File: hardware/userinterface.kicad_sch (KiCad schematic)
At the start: 16 parts, among them J3 NHD-2.4-240320AF-CSXP, SW3 L-KLS4-EC1121S-E5A-F12.5, U7 TPS61023DRLR, U8 CAT4104V-GT3

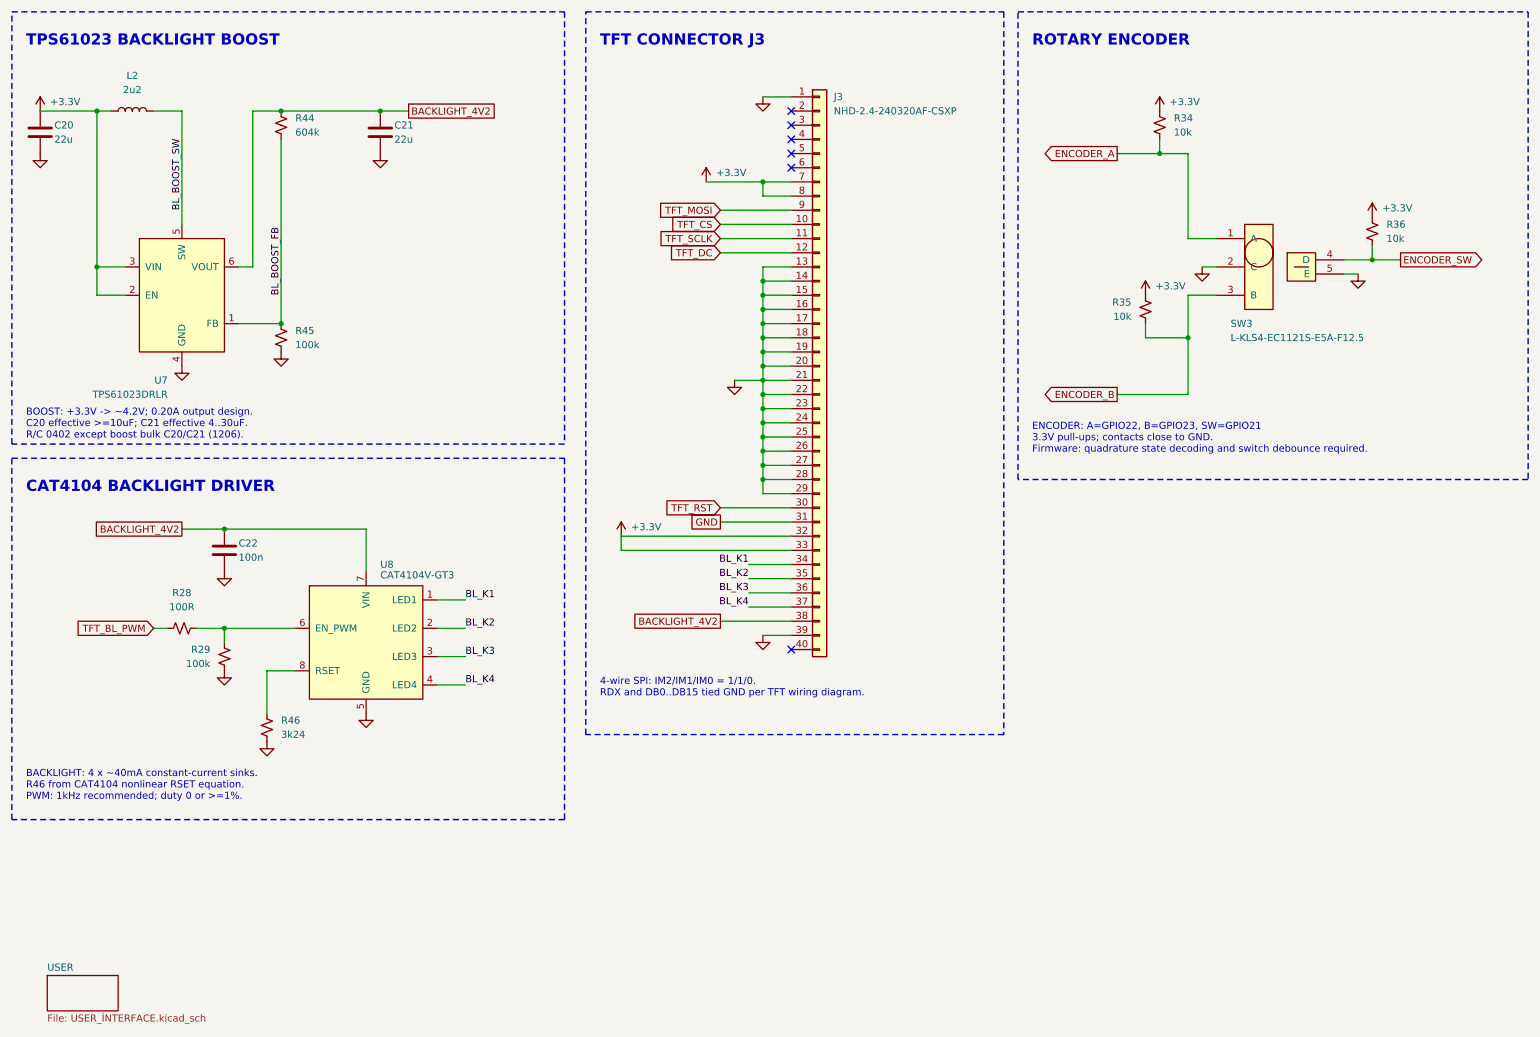
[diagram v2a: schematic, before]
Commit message: hardware: ekranı TFT032B018'e geçir, todo'yu güncelle, Imax 3 A kararını kaydet
TFT032B018 (userinterface):
- J3 Conn_01x40 (Molex 54132-4062) -> Conn_01x30, KLS L-KLS1-242I-2.0-30-R;
  yeni footprint Connector_FPC_Custom:KLS_L-KLS1-242I-2.0-30_1x30-2MP_P0.50mm_Horizontal
  (fp-lib-table'a eklendi). SPI: 16=DC, 17=SCLK, 18=CS, 19=MOSI, 20=RST;
  21 IM=3.3V; DB0..7, RDX GND; TE ve dokunmatik pinleri boş. C34 1u0 dekuplaj.
- Backlight: TPS61023 boost (U7, L2, C20, C21, R44, R45) ve CAT4104 (U8,
  C22, R46) kalktı; +3.3V -> R60 5R6 -> BL_A, BL_K -> Q7 IRLML6344
  (R28/R29 ile TFT_BL_PWM).
- Beklenen netlist farkı: BACKLIGHT_4V2, BL_BOOST_*, BL_K1..4, Net-(U8-*)
  kalktı; BL_A, BL_K, Net-(Q7-G) eklendi; TFT_* netleri J3'ün yeni pin
  numaralarına geçti. ERC değişmedi (0 hata, 2 eski uyarı).
- Özdisan alanları (J3, Q7, R60, C34) ve BOM tablosu güncellendi; ekran modülü
  şema dışı satır olarak BOM'da (stok 5).
- mcu/userinterface: kullanılmayan lib_symbols tanımları silindi
  (Device:Battery_Cell, AO3400A); netlist farkı YOK.

Kayıtlar:
- todo.txt: tamamlanan şema maddeleri
  design_decisions/output/SEMA_TAMAMLANAN_TODO_REV_C_20260922.md'ye taşındı;
  AP74502Q sembolü Diodes datasheet'iyle doğrulandı (datasheet eklendi),
  U12 paket (SOT28) kontrolü ve SMBJ30A PCB maddesi güncellendi.
- Maksimum çıkış akımı 3 A: design_decisions/output/CIKIS_AKIMI_3A_KARARI_20260922.md.
  "Imax kesinleştir" ve "3.3 V adaptör başlığı" maddeleri kapandı; prototip ve
  INA226 firmware değerleri 3 A'e göre güncellendi, RShunt1 5 mOhm'da kaldı.

Co-Authored-By: Claude Opus 5 <noreply@anthropic.com>
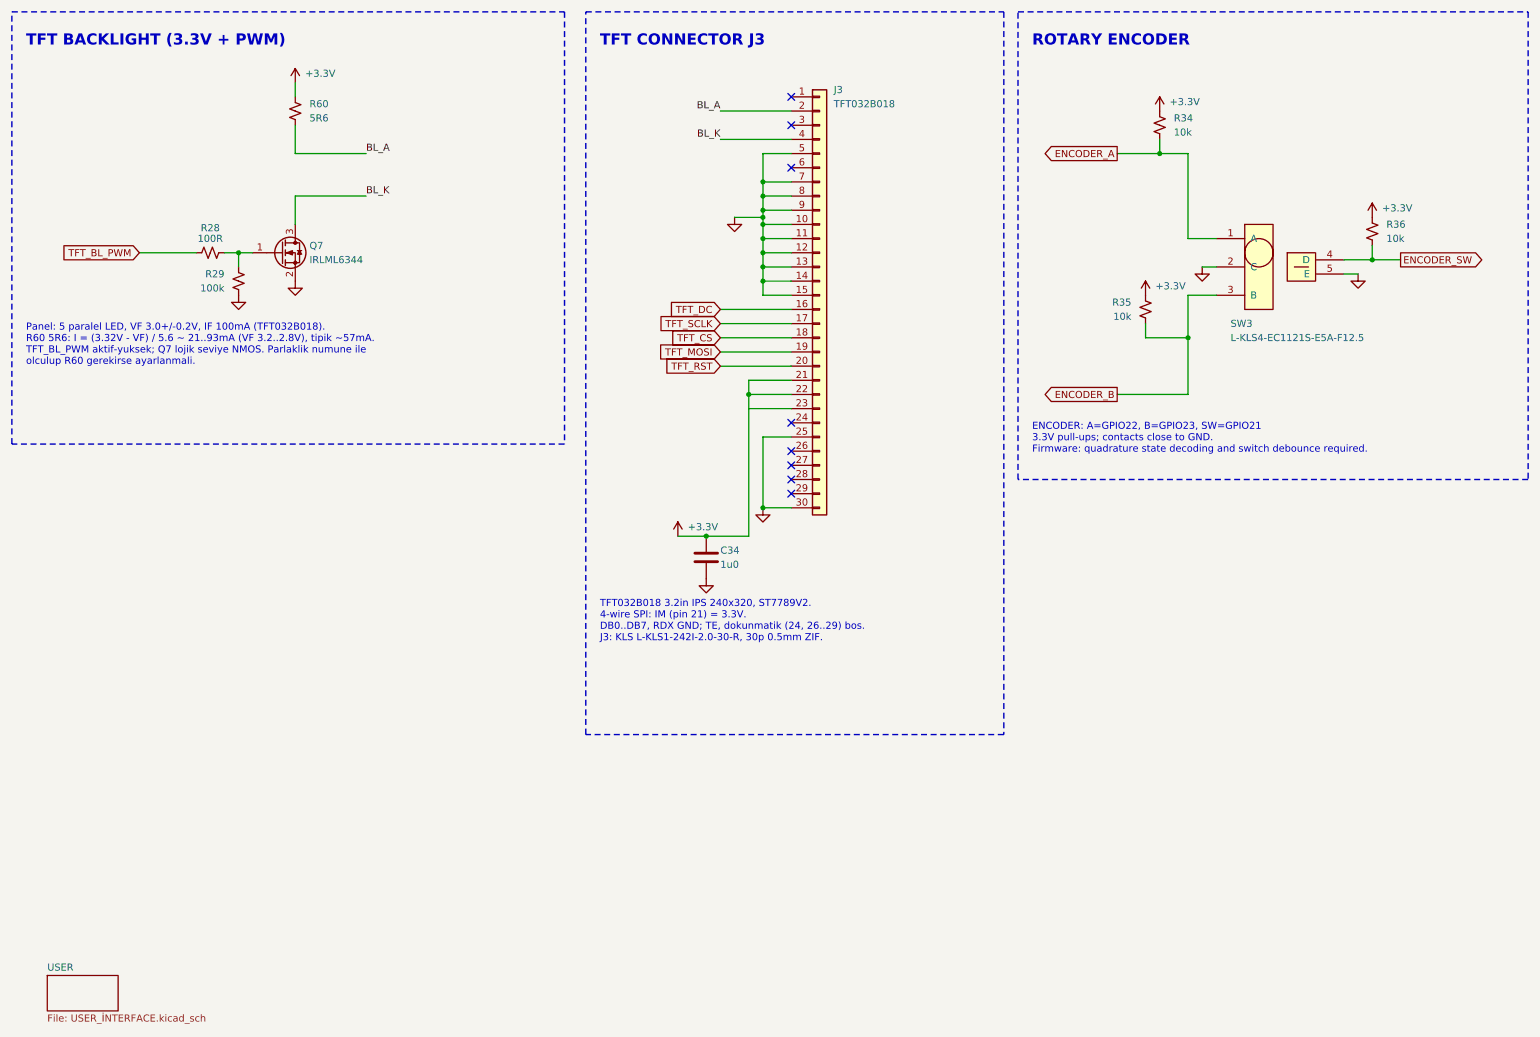
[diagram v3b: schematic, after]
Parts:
- removed C20, C21: 22u, Capacitor_SMD:C_0805_2012Metric, symbol Device:C
- removed C22: 100n, Capacitor_SMD:C_0402_1005Metric, symbol Device:C
- removed L2: 2u2, Inductor_SMD:L_Wuerth_MAPI-4030, symbol Device:L
- removed R44: 604k, Resistor_SMD:R_0402_1005Metric, symbol Device:R_Small_US
- removed R45: 100k, Resistor_SMD:R_0402_1005Metric, symbol Device:R_Small_US
- removed R46: 3k24, Resistor_SMD:R_0402_1005Metric, symbol Device:R_Small_US
- removed U7: TPS61023DRLR, Power_Management_Custom:TPS61023_DRL0006A, symbol Power_Supply_Custom:TPS61023DRLR
- removed U8: CAT4104V-GT3, Package_SO:SOIC-8_3.9x4.9mm_P1.27mm, symbol Power_Supply_Custom:CAT4104V-GT3
- added C34: 1u0, Capacitor_SMD:C_0402_1005Metric, symbol Device:C
- added Q7: IRLML6344, Package_TO_SOT_SMD:SOT-23, symbol Transistor_FET:Q_NMOS_GSD
- added R60: 5R6, Resistor_SMD:R_0805_2012Metric, symbol Device:R_Small_US
- J3: value NHD-2.4-240320AF-CSXP -> TFT032B018; footprint Molex_541324062:CON_541324062_MOL -> Connector_FPC_Custom:KLS_L-KLS1-242I-2.0-30_1x30-2MP_P0.50mm_Horizontal; symbol Connector_Generic:Conn_01x40 -> Connector_Generic:Conn_01x30; ConnectorType Receptacle -> FFC/FPC Receptacle, flip ZIF, double contact; ContactPlating TBD -> Tin/Gold (phosphor bronze); DesignNote TFT modulu (NHD-2.4-240320AF-CSXP) bu konnektore takilir; m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 -> TFT032B018 (3.2in IPS, ST7789V2) FPC konnektoru. SPI: 16=DC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; Height TBD -> 2.0mm; MPN 54132-4062 -> L-KLS1-242I-2.0-30-R; Manufacturer Molex -> KLS Electronic; OperatingTemp TBD -> -25C to 85C; Orientation TBD -> Horizontal (right angle); Package FPC 0.5mm 40-pos SMD -> FPC 0.5mm 30-pos SMD ZIF; PositionCount 40 -> 30; RoHS TBD -> Yes; SelectionNote Özdisan 1325143; stok 13297 (21.09.2026); Uygun. 21.09 ikin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 -> Özdisan 695049; stok 1248 (21.09.2026); Uygun. 22.09 TFT032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; Series TBD -> KLS1-242I; VoltageRating TBD -> 50V
- R28: DesignNote TBD -> Q7 kapi seri direnci.
- R29: DesignNote TBD -> Q7 kapi pull-down; ESP32 acilisinda backlight kapali.
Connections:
- net +3.3V: now also J3.21 (Pin_21), J3.22 (Pin_22), J3.23 (Pin_23), C34.1, R60.1; no longer J3.32 (Pin_32), J3.33 (Pin_33), J3.7 (Pin_7), J3.8 (Pin_8)
- net GND: now also J3.10 (Pin_10), J3.11 (Pin_11), J3.12 (Pin_12), J3.30 (Pin_30), J3.5 (Pin_5), J3.7 (Pin_7), J3.8 (Pin_8), J3.9 (Pin_9), C34.2, Q7.2 (S); no longer J3.1 (Pin_1), J3.16 (Pin_16), J3.17 (Pin_17), J3.18 (Pin_18), J3.19 (Pin_19), J3.20 (Pin_20), J3.21 (Pin_21), J3.22 (Pin_22), J3.23 (Pin_23), J3.24 (Pin_24), J3.26 (Pin_26), J3.27 (Pin_27), J3.28 (Pin_28), J3.29 (Pin_29), J3.31 (Pin_31), J3.39 (Pin_39)
- net TFT_CS: now also J3.18 (Pin_18); no longer J3.10 (Pin_10)
- net TFT_DC: now also J3.16 (Pin_16); no longer J3.12 (Pin_12)
- net TFT_MOSI: now also J3.19 (Pin_19); no longer J3.9 (Pin_9)
- net TFT_RST: now also J3.20 (Pin_20); no longer J3.30 (Pin_30)
- net TFT_SCLK: now also J3.17 (Pin_17); no longer J3.11 (Pin_11)
- net at R28.2, R29.1: now also Q7.1 (G)
- net BL_A: now reaches J3.2 (Pin_2)
- net BL_A: now also R60.2
- net BL_K: now reaches J3.4 (Pin_4)
- net BL_K: now also Q7.3 (D)
- removed net BACKLIGHT_4V2: J3.38 (Pin_38)
- removed net BL_K1: J3.34 (Pin_34)
- removed net BL_K2: J3.35 (Pin_35)
- removed net BL_K3: J3.36 (Pin_36)
- removed net BL_K4: J3.37 (Pin_37)
- no-connect marks 6 -> 8
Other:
- note added: "Panel: 5 paralel LED, VF 3.0+/-0.2V, IF 100mA (TFT032B018). R60 5R6: I = (3.32V - VF) / 5.6 ~ 21..93mA (VF 3.2..2.8V), tipik ~57mA. TFT_BL_PWM aktif-yuksek; Q7 lojik seviye NMOS. Parlaklik numune ile olculup R60 gerekirse ayarlanmali."
- note added: "TFT BACKLIGHT (3.3V + PWM)"
- note added: "TFT032B018 3.2in IPS 240x320, ST7789V2. 4-wire SPI: IM (pin 21) = 3.3V. DB0..DB7, RDX GND; TE, dokunmatik (24, 26..29) bos. J3: KLS L-KLS1-242I-2.0-30-R, 30p 0.5mm ZIF."
- note removed: "4-wire SPI: IM2/IM1/IM0 = 1/1/0. RDX and DB0..DB15 tied GND per TFT wiring diagram."
- note removed: "BACKLIGHT: 4 x ~40mA constant-current sinks. R46 from CAT4104 nonlinear RSET equation. PWM: 1kHz recommended; duty 0 or >=1%."
- note removed: "BOOST: +3.3V -> ~4.2V; 0.20A output design. C20 effective >=10uF; C21 effective 4..30uF. R/C 0402 except boost bulk C20/C21 (1206)."
- note removed: "CAT4104 BACKLIGHT DRIVER"
- note removed: "TPS61023 BACKLIGHT BOOST"
- moved on the sheet: R28, R29

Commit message: hardware: U2'yi ESP32-C6-MINI-1-H4'e geçir, şema notlarını güncelle (TASK-041/004/005)
TASK-041 — U2 ESP32-C6-WROOM-1 -> ESP32-C6-MINI-1-H4 (4 MB flash, -40..105 C,
13,2x16,6 mm). Modül IO10/IO11'i dışarı vermiyor (datasheet v1.5 Tablo 3-1):
- TFT_CS GPIO10 -> GPIO14 (pin 19), TFT_DC GPIO11 -> GPIO7 (pin 16).
- Kullanılan GPIO 0-9 ve 12-23; modülün verdiği kümeyle birebir örtüşüyor,
  boşta GPIO kalmadı. Strapping (4/5/8/9/15) rolleri değişmedi.
- Sembol/footprint KiCad standart kütüphanesinden: RF_Module:ESP32-C6-MINI-1.
- IO8/IO9 MINI-1'de sol kenarda: R37/R15/TP9 ve R10/SW1 U2'nin soluna taşındı,
  iki pull-up tek +3.3V rayını paylaşıyor (#PWR023 kalktı).
- USB seri dirençleri yerinde kaldı, taşıdıkları sinyal yer değiştirdi
  (R2 -> D-, R3 -> D+; USB_DM/USB_DP etiketleri satır değiştirdi).
- Netlist: her net U2 dışındaki üyelerini korudu (yalnız pin numaraları
  değişti), GND'ye modülün tüm toprak pedleri katıldı.

TASK-004 — Eskiyen şema notları: AOZ1284 bloğunda COMP değerleri (Rc=51k,
Cc=15n -> fC ~20 kHz), seçilen L1/D2/Cout parçaları ve "Cout: 10V X7R" hatası
düzeltildi; blok başlığı "V_PRE 5..28V INPUT" oldu. mcu sayfasında çerçeve
dışında kalmış altı eski inceleme sorusu kaldırıldı. Diğer sayfalar tarandı,
güncel.

TASK-005 — USER_İNTERFACE.kicad_sch kaldırıldı (dosya + sayfa sembolü +
.kicad_pro kaydı). İçindeki arayüz sinyal listesi docs/arayuz-sinyalleri.md'ye
güncel pin atamalarıyla taşındı. Sayfa sayısı 6 -> 5.

Doğrulama: ERC 0 hata / 0 uyarı; not/sayfa değişikliklerinde netlist farkı YOK;
okunabilirlik denetiminde yeni bulgu yok (kalan 3 bulgu eskiden beri var).

Ayrıca: TASK-006 footprint listesi güncellendi, TASK-042 açıldı (PCB
güncellemesinden sonra kullanılmayan PCM_Espressif kütüphanesini kaldır),
software/FIRMWARE_GEREKSINIMLERI.md pin haritası yenilendi.

Co-Authored-By: Claude Opus 5 <noreply@anthropic.com>
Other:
- removed sheet USER
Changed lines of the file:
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@@
-		)
-	)
-	(sheet
-		(at 19.05 185.42)
-		(size 12.7 6.35)
-		(exclude_from_sim no)
-		(in_bom yes)
-		(on_board yes)
-		(dnp no)
-		(fields_autoplaced yes)
-		(stroke
-			(width 0.1524)
-			(type solid)
-			(color 255 11 240 1)
-		)
-		(fill
-			(color 255 9 212 1)
-		)
-		(property "Sheetname" "USER"
-			(at 19.05 184.7084 0)
-			(show_name no)
-			(do_not_autoplace no)
-			(effects
-				(font
-					(size 1.27 1.27)
-				)
-				(justify left bottom)
-			)
-		)
-		(property "Sheetfile" "USER_İNTERFACE.kicad_sch"
-			(at 19.05 192.3546 0)
-			(show_name no)
-			(do_not_autoplace no)
-			(effects
-				(font
-					(size 1.27 1.27)
-				)
-				(justify left top)
-			)
-		)
-		(instances
-			(project "gopo"
-				(path "/a43081a6-9aa2-4898-9347-bbcb5849dafd/f0e4530d-2b12-46bf-98ff-bd44498f317b"
-					(page "12")
-				)
-			)
 		)
 	)
